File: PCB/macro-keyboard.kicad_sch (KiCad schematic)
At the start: 36 parts, among them SW1 SW_Push, SW2 SW_Push, SW3 SW_Push, SW4 SW_Push, SW5 SW_Push, SW6 SW_Push, SW7 SW_Push, SW8 SW_Push, U1 PRTR5V0U2X, U2 ATmega32U4-A, Y1 Crystal_GND24_Small

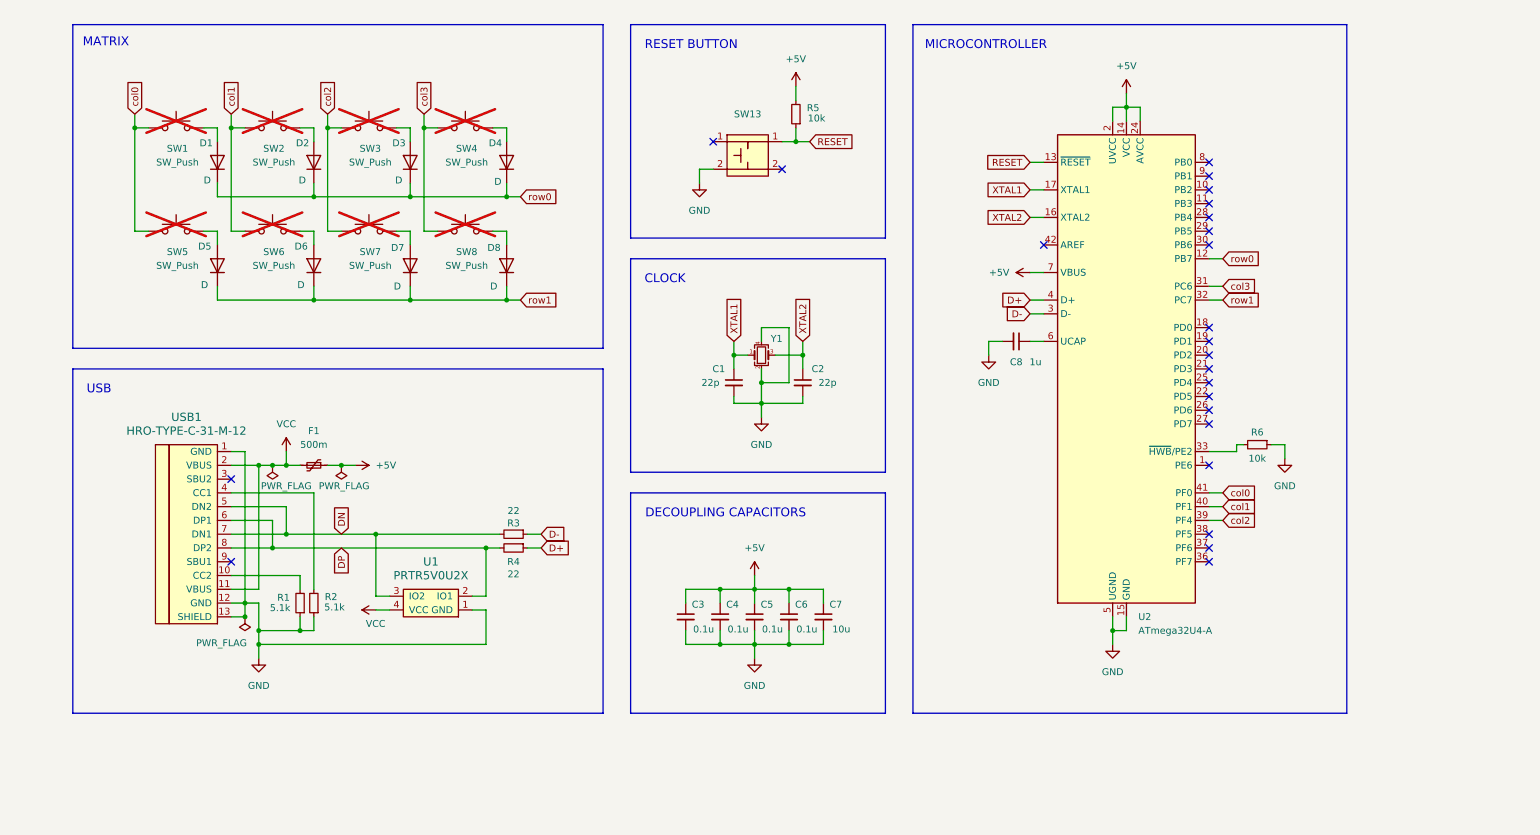
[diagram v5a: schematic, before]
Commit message: Significantly simplify design
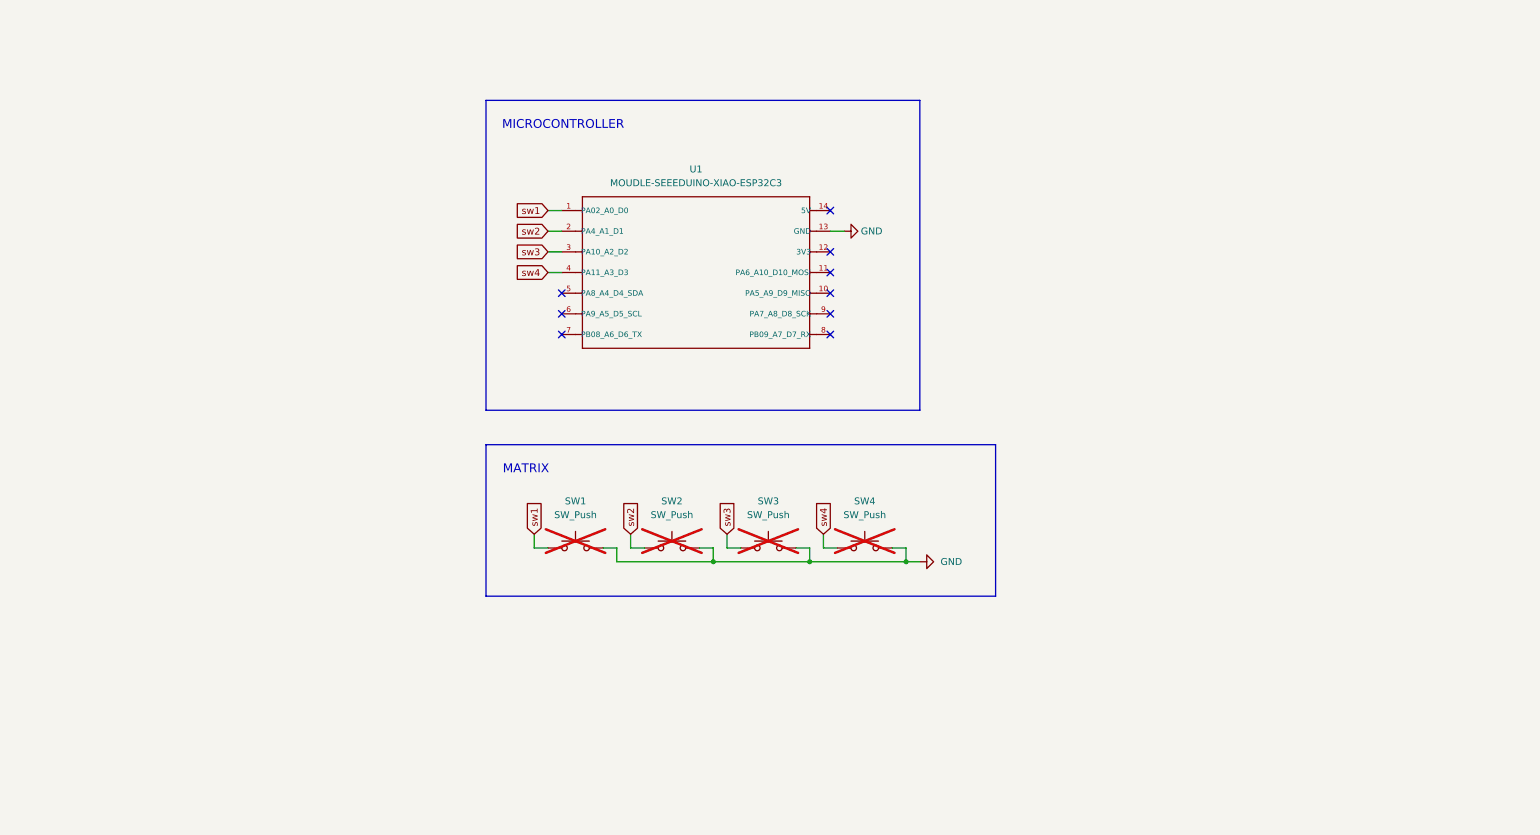
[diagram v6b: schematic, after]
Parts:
- removed C1, C2: 22p, Capacitor_SMD:C_0805_2012Metric_Pad1.18x1.45mm_HandSolder, symbol Device:C_Small
- removed C3, C4, C5, C6: 0.1u, Capacitor_SMD:C_0805_2012Metric_Pad1.18x1.45mm_HandSolder, symbol Device:C_Small
- removed C7: 10u, Capacitor_SMD:C_0805_2012Metric_Pad1.18x1.45mm_HandSolder, symbol Device:C_Small
- removed C8: 1u, Capacitor_SMD:C_0805_2012Metric_Pad1.18x1.45mm_HandSolder, symbol Device:C_Small
- removed D1, D2, D3, D4, D5, D6, D7, D8: D, Diode_SMD:D_SOD-123, symbol Device:D
- removed F1: 500m, Fuse:Fuse_1206_3216Metric_Pad1.42x1.75mm_HandSolder, symbol Device:Polyfuse_Small
- removed R1, R2: 5.1k, Resistor_SMD:R_0805_2012Metric_Pad1.20x1.40mm_HandSolder, symbol Device:R_Small
- removed R3, R4: 22, Resistor_SMD:R_0805_2012Metric_Pad1.20x1.40mm_HandSolder, symbol Device:R_Small
- removed R5, R6: 10k, Resistor_SMD:R_0805_2012Metric_Pad1.20x1.40mm_HandSolder, symbol Device:R_Small
- removed SW13: ~, Button_Switch_SMD:SW_SPST_SKQG_WithStem, symbol local:SW_SKQG
- removed SW5, SW6, SW7, SW8: SW_Push, ScottoKeebs_MX:MX_PCB_1.00u, symbol Switch:SW_Push
- removed U1: PRTR5V0U2X, random-keyboard-parts:SOT143B, symbol random-keyboard-parts:PRTR5V0U2X
- removed U2: ATmega32U4-A, Package_QFP:TQFP-44_10x10mm_P0.8mm, symbol MCU_Microchip_ATmega:ATmega32U4-A
- removed USB1: HRO-TYPE-C-31-M-12, Type-C:HRO-TYPE-C-31-M-12-HandSoldering, symbol Type-C:HRO-TYPE-C-31-M-12
- removed Y1: Crystal_GND24_Small, Crystal:Crystal_SMD_3225-4Pin_3.2x2.5mm_HandSoldering, symbol Device:Crystal_GND24_Small
- added U1: MOUDLE-SEEEDUINO-XIAO-ESP32C3, MOUDLE14P-SMD-2.54-21X17.8MM, symbol MOUDLE-SEEEDUINO-XIAO-ESP32C3:MOUDLE-SEEEDUINO-XIAO-ESP32C3
- SW1, SW2, SW3, SW4: footprint ScottoKeebs_MX:MX_PCB_1.00u -> MX_Only:MXOnly-1U-Hotswap
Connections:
- net GND: now also SW1.2, SW2.2, SW3.2, SW4.2, U1.13 (GND)
- net col0 renamed sw1
- net sw1: now also U1.1 (PA02_A0_D0)
- net col1 renamed sw2
- net sw2: now also U1.2 (PA4_A1_D1)
- net col2 renamed sw3
- net sw3: now also U1.3 (PA10_A2_D2)
- net col3 renamed sw4
- net sw4: now also U1.4 (PA11_A3_D3)
- no-connect marks 24 -> 9
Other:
- note removed: "CLOCK"
- note removed: "DECOUPLING CAPACITORS"
- note removed: "RESET BUTTON"
- note removed: "USB"
- moved on the sheet: SW1, SW2, SW3, SW4

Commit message: Convert to use seeed studio xiao samd21
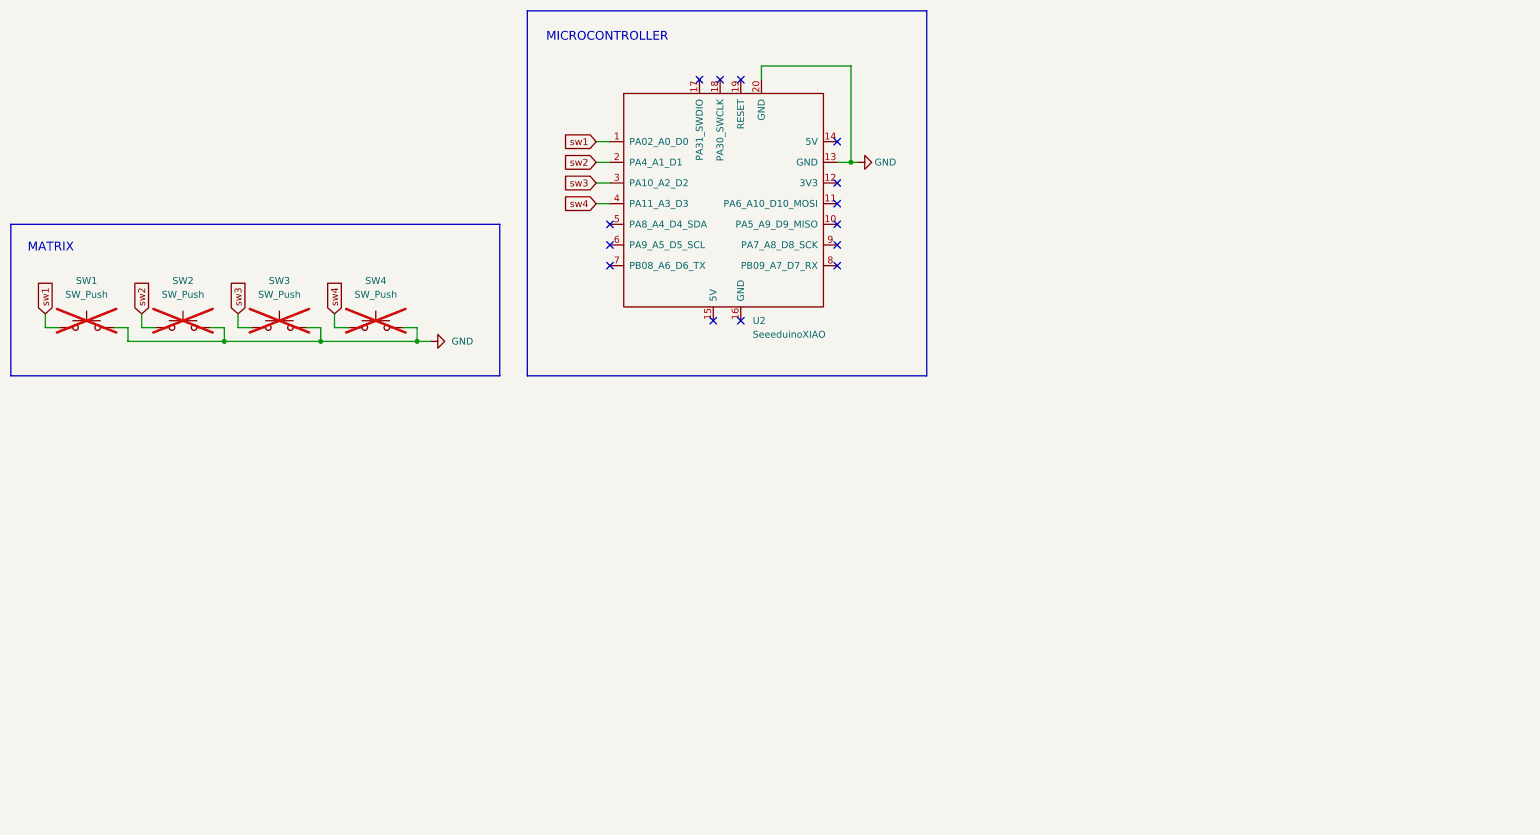
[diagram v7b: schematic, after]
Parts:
- removed U1: MOUDLE-SEEEDUINO-XIAO-ESP32C3, MOUDLE14P-SMD-2.54-21X17.8MM, symbol MOUDLE-SEEEDUINO-XIAO-ESP32C3:MOUDLE-SEEEDUINO-XIAO-ESP32C3
- added U2: SeeeduinoXIAO, Seeeduino XIAO KICAD:Seeeduino XIAO-MOUDLE14P-2.54-21X17.8MM, symbol Seeeduino XIAO:SeeeduinoXIAO
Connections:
- net GND: now also U2.13 (GND), U2.20 (GND)
- net sw1: now also U2.1 (PA02_A0_D0)
- net sw2: now also U2.2 (PA4_A1_D1)
- net sw3: now also U2.3 (PA10_A2_D2)
- net sw4: now also U2.4 (PA11_A3_D3)
- no-connect marks 9 -> 14
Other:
- moved on the sheet: SW1, SW2, SW3, SW4

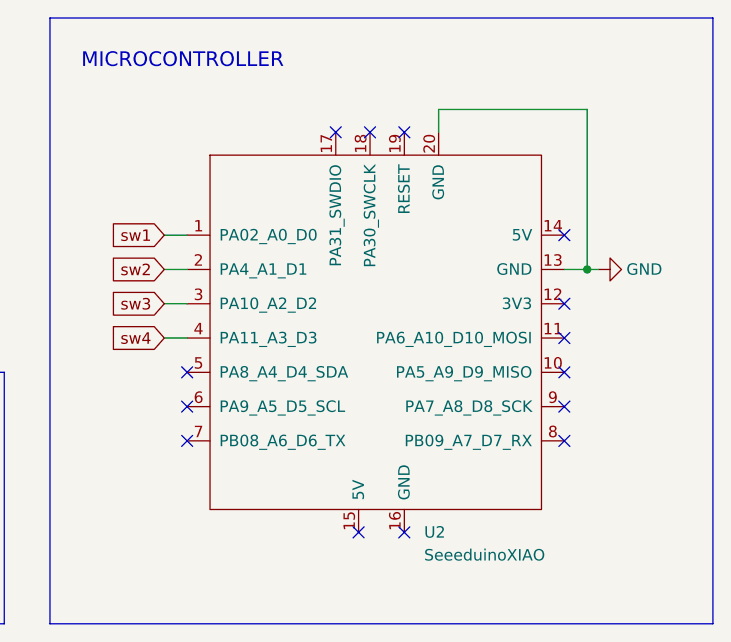
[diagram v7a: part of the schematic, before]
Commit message: Update case for simplified design
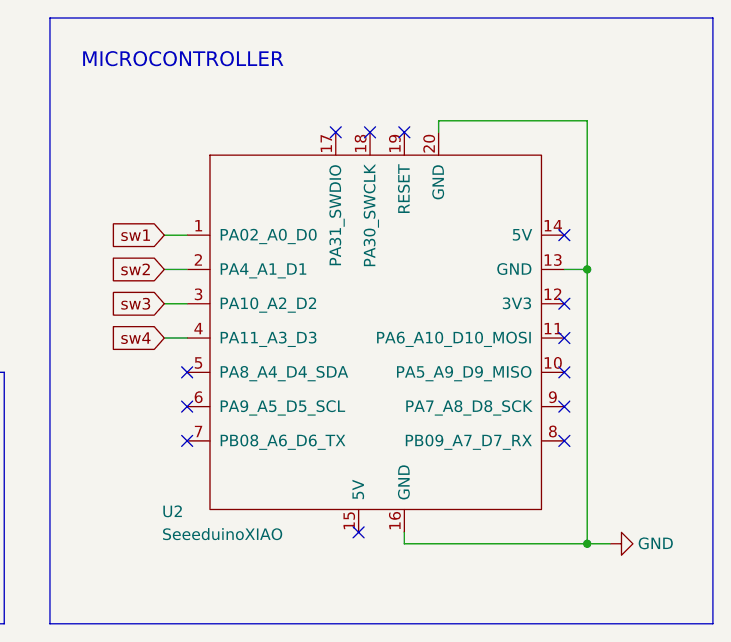
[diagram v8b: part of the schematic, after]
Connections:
- net GND: now also U2.16 (GND)
- no-connect marks 14 -> 13
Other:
- title: Macro Keyboard 2x4 -> Macro Keyboard 4x1
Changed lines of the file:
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@@
 	(paper "A5")
 	(title_block
-		(title "Macro Keyboard 2x4")
+		(title "Macro Keyboard 4x1")
 		(date "2025-01-22")
-		(rev "0.1")
+		(rev "0.2")
 	)
 	(junction
@@
 	)
 	(junction
-		(at 175.26 53.34)
+		(at 175.26 83.82)
 		(diameter 0)
 		(color 0 0 0 0)
@@
 		(color 0 0 0 0)
 	)
-	(no_connect
-		(at 154.94 82.55)
+	(junction
+		(at 175.26 53.34)
+		(diameter 0)
+		(color 0 0 0 0)
 	)
 	(no_connect
@@
 	(wire
 		(pts
-			(xy 158.75 38.1) (xy 158.75 35.56)
-		)
-		(stroke
-			(width 0)
-			(type default)
-		)
-	)
-	(wire
-		(pts
 			(xy 128.27 49.53) (xy 130.81 49.53)
 		)
@@
 	(wire
 		(pts
-			(xy 158.75 35.56) (xy 175.26 35.56)
+			(xy 177.8 83.82) (xy 175.26 83.82)
+		)
+		(stroke
+			(width 0)
+			(type default)
+		)
+	)
+	(wire
+		(pts
+			(xy 154.94 82.55) (xy 154.94 83.82)
 		)
 		(stroke
@@
 	(wire
 		(pts
+			(xy 158.75 38.1) (xy 158.75 36.83)
+		)
+		(stroke
+			(width 0)
+			(type default)
+		)
+	)
+	(wire
+		(pts
+			(xy 158.75 36.83) (xy 175.26 36.83)
+		)
+		(stroke
+			(width 0)
+			(type default)
+		)
+	)
+	(wire
+		(pts
 			(xy 95.25 86.36) (xy 97.79 86.36)
 		)
@@
 	(wire
 		(pts
+			(xy 175.26 36.83) (xy 175.26 53.34)
+		)
+		(stroke
+			(width 0)
+			(type default)
+		)
+	)
+	(wire
+		(pts
 			(xy 77.47 83.82) (xy 77.47 86.36)
 		)
@@
 	(wire
 		(pts
+			(xy 175.26 83.82) (xy 175.26 53.34)
+		)
+		(stroke
+			(width 0)
+			(type default)
+		)
+	)
+	(wire
+		(pts
 			(xy 41.91 83.82) (xy 41.91 86.36)
 		)
@@
 	(wire
 		(pts
-			(xy 175.26 53.34) (xy 176.53 53.34)
-		)
-		(stroke
-			(width 0)
-			(type default)
-		)
-	)
-	(wire
-		(pts
 			(xy 29.21 83.82) (xy 26.67 83.82)
 		)
@@
 	(wire
 		(pts
+			(xy 154.94 83.82) (xy 175.26 83.82)
+		)
+		(stroke
+			(width 0)
+			(type default)
+		)
+	)
+	(wire
+		(pts
 			(xy 74.93 83.82) (xy 77.47 83.82)
-		)
-		(stroke
-			(width 0)
-			(type default)
-		)
-	)
-	(wire
-		(pts
-			(xy 175.26 35.56) (xy 175.26 53.34)
 		)
 		(stroke
@@
 	(symbol
 		(lib_id "power:GND")
-		(at 176.53 53.34 90)
+		(at 177.8 83.82 90)
 		(unit 1)
 		(exclude_from_sim no)
@@
 		(dnp no)
 		(property "Reference" "#PWR01"
-			(at 182.88 53.34 0)
+			(at 184.15 83.82 0)
 			(effects
 				(font
@@
 		)
 		(property "Value" "GND"
-			(at 181.61 53.34 90)
+			(at 182.88 83.82 90)
 			(effects
 				(font
@@
 		)
 		(property "Footprint" ""
-			(at 176.53 53.34 0)
+			(at 177.8 83.82 0)
 			(effects
 				(font
@@
 		)
 		(property "Datasheet" ""
-			(at 176.53 53.34 0)
+			(at 177.8 83.82 0)
 			(effects
 				(font
@@
 		)
 		(property "Description" "Power symbol creates a global label with name \"GND\" , ground"
-			(at 176.53 53.34 0)
+			(at 177.8 83.82 0)
 			(effects
 				(font
@@
 		(on_board yes)
 		(dnp no)
-		(fields_autoplaced yes)
 		(property "Reference" "U2"
-			(at 157.1341 82.55 0)
+			(at 128.016 80.264 0)
 			(effects
 				(font
@@
 		)
 		(property "Value" "SeeeduinoXIAO"
-			(at 157.1341 85.09 0)
-			(effects
-				(font
+			(at 128.016 82.804 0)
+			(effects
+				(font
